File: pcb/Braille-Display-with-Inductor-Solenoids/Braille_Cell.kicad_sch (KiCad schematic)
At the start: 43 parts, among them U10 AD116, U11 AD116, U12 AD116, U13 AD116, U8 AD116, U9 AD116

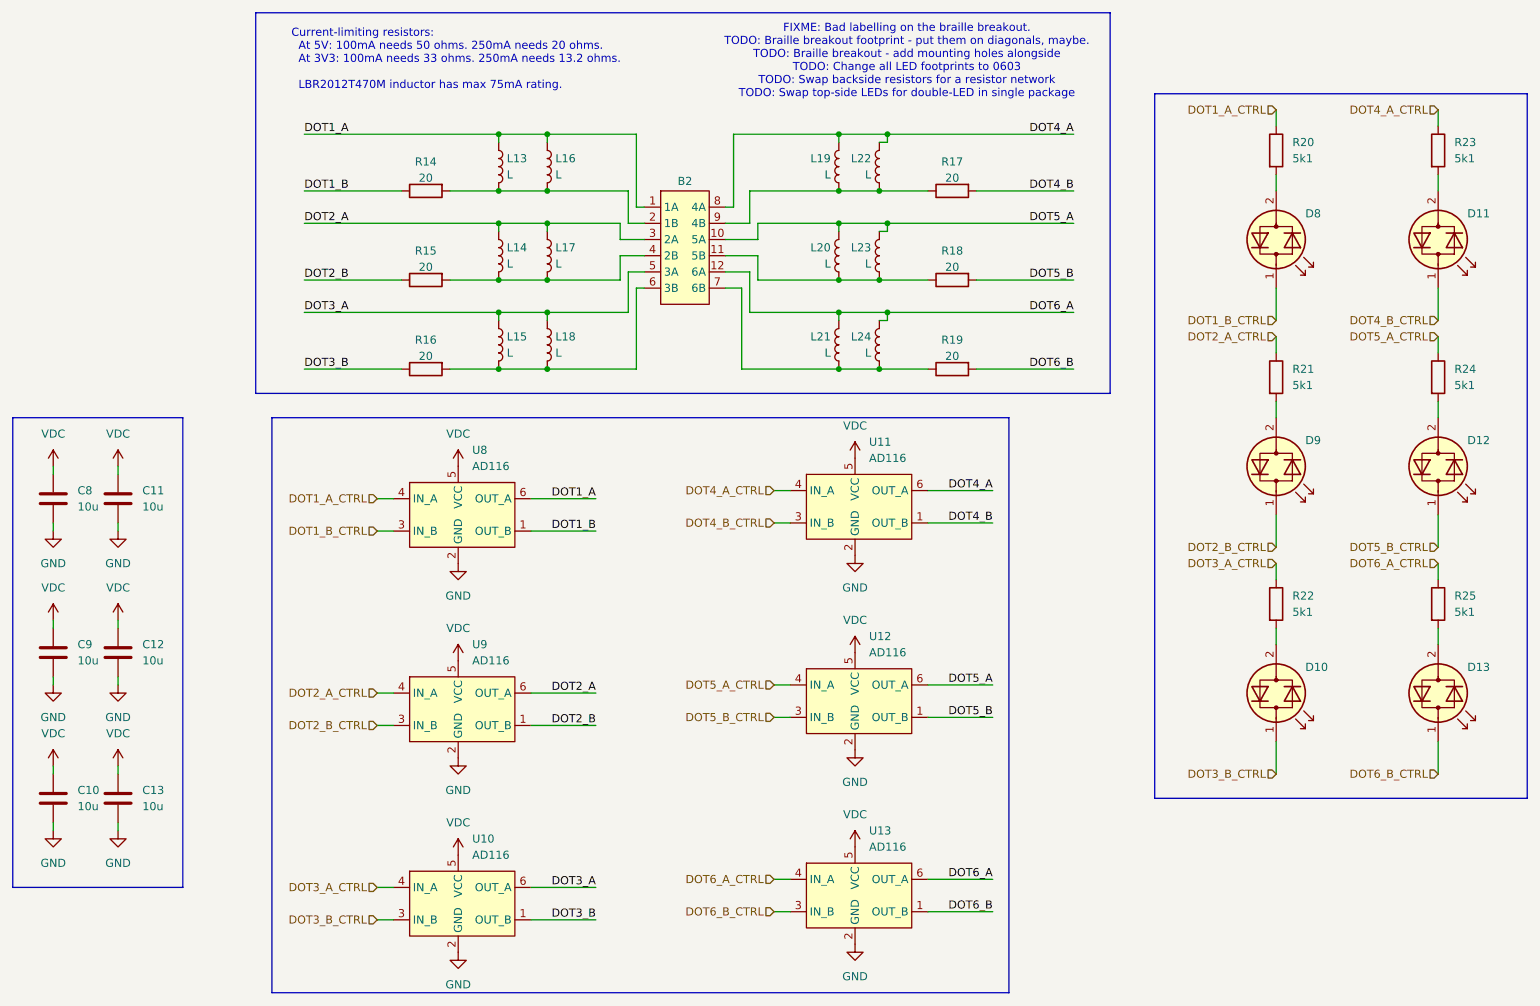
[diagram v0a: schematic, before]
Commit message: PCB (Rev 3): Switch to 2 inductors per cell (#2)
* WIP (Rev3): Switch to 2 inductors per cell

* WIP: Route one cell

* WIP: Route more of the board

* WIP: Swap around power input placement

* Finish and polish design

* Bit of tiny routing, export production file
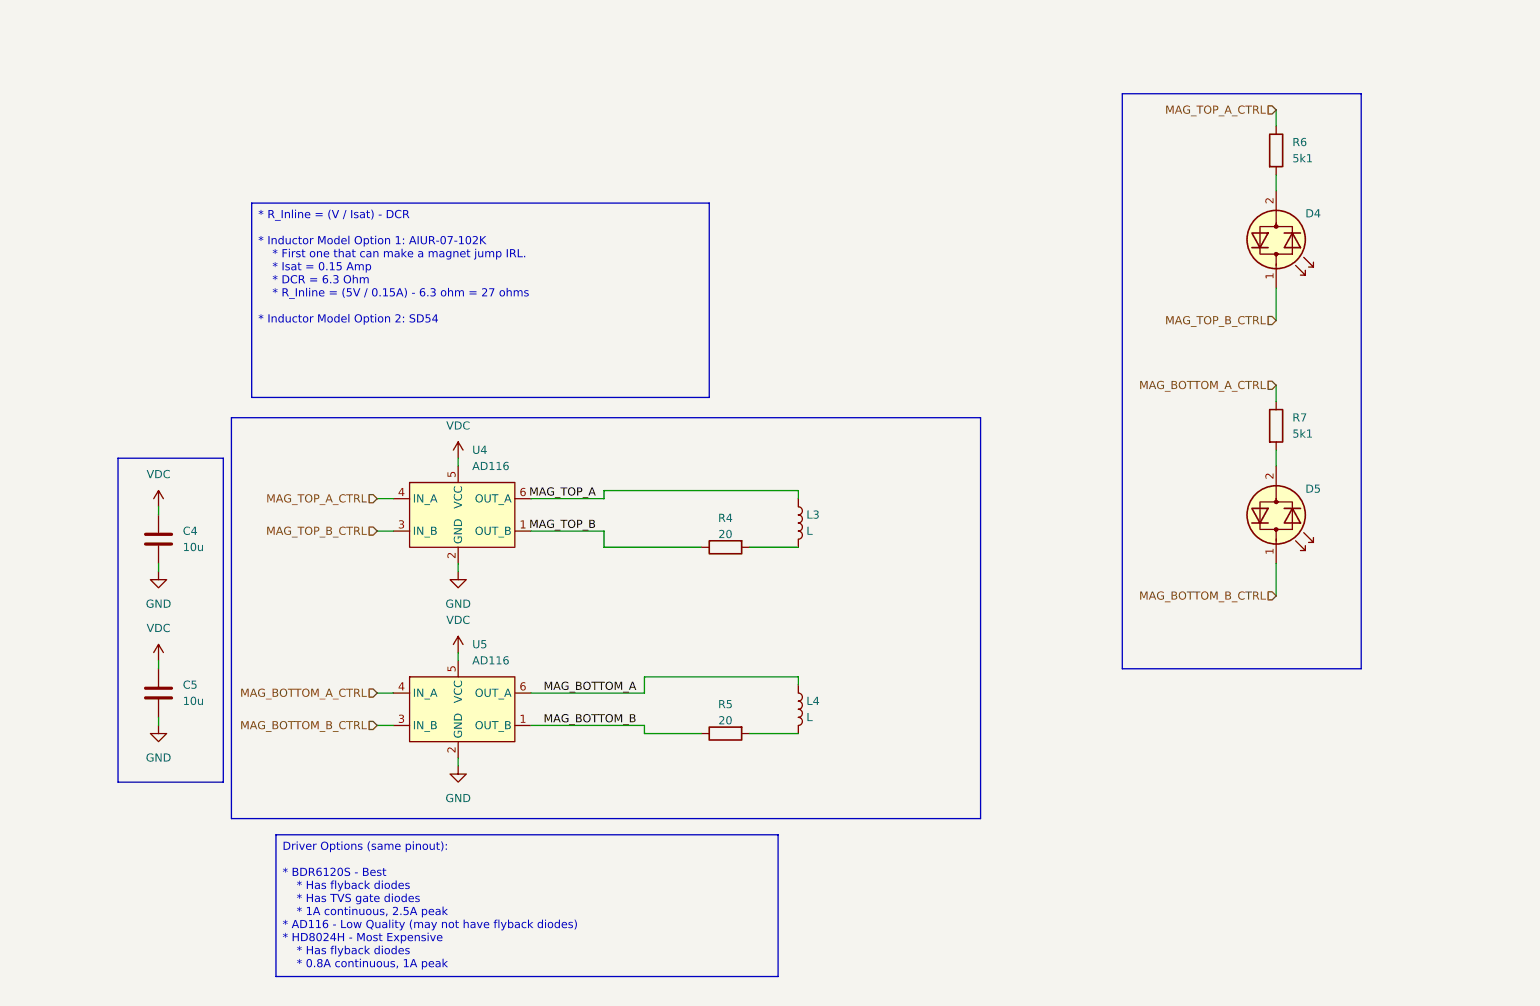
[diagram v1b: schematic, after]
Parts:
- removed B2: ~, 00-project-footprints:Braille_Cell_Breakout, symbol 00-project-symbols:Braille_Cell_Breakout
- removed C10, C11, C12, C13: 10u, Capacitor_SMD:C_1206_3216Metric_Pad1.33x1.80mm_HandSolder, symbol Device:C
- removed D10, D11, D12, D13: LED_Dual_Bidirectional, 00-project-footprints:LED_0603_1608Metric_HandSolder_2x_Reverse, symbol Device:LED_Dual_Bidirectional
- removed L15, L22, L23, L24: L, 00-project-footprints:Inductor_0805_2012Metric_SMD_Vertical_Square_Rev2_1.3mm, symbol Device:L
- removed L16, L17, L18, L19, L20, L21: L, 00-project-footprints:Inductor_VLS201612CX, symbol Device:L
- removed R16, R17, R18, R19: 20, Resistor_SMD:R_0603_1608Metric_Pad0.98x0.95mm_HandSolder, symbol Device:R
- removed R22, R23, R24, R25: 5k1, Resistor_SMD:R_0603_1608Metric_Pad0.98x0.95mm_HandSolder, symbol Device:R
- removed U10, U11, U12, U13: AD116, Package_TO_SOT_SMD:SOT-23-6, symbol 00-project-symbols:AD116_H_Bridge
- L3: renamed from L13; footprint 00-project-footprints:Inductor_0805_2012Metric_SMD_Vertical_Square_Rev2_1.3mm -> 00-project-footprints:Inductor_6mm_AIUR-07-102K_THT_SD54_SMD
- L4: renamed from L14; footprint 00-project-footprints:Inductor_0805_2012Metric_SMD_Vertical_Square_Rev2_1.3mm -> 00-project-footprints:Inductor_6mm_AIUR-07-102K_THT_SD54_SMD
- R4: renamed from R14; footprint Resistor_SMD:R_0603_1608Metric_Pad0.98x0.95mm_HandSolder -> Resistor_SMD:R_2512_6332Metric_Pad1.40x3.35mm_HandSolder
- R5: renamed from R15; footprint Resistor_SMD:R_0603_1608Metric_Pad0.98x0.95mm_HandSolder -> Resistor_SMD:R_2512_6332Metric_Pad1.40x3.35mm_HandSolder
- renumbered C8 to C4, C9 to C5, D8 to D4, D9 to D5, R20 to R6, R21 to R7, U8 to U4, U9 to U5
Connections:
- net DOT1_A renamed MAG_TOP_A
- net DOT1_A_CTRL renamed MAG_TOP_A_CTRL
- net DOT1_B renamed MAG_TOP_B
- net DOT1_B_CTRL renamed MAG_TOP_B_CTRL
- net DOT2_A renamed MAG_BOTTOM_A
- net DOT2_A_CTRL renamed MAG_BOTTOM_A_CTRL
- net DOT2_B renamed MAG_BOTTOM_B
- net DOT2_B_CTRL renamed MAG_BOTTOM_B_CTRL
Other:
- note removed: "Current-limiting resistors: At 5V: 100mA needs 50 ohms. 250mA needs 20 ohms. At 3V3: 100mA needs 33 ohms. 250mA needs 13.2 ohms. LBR2012T470M inductor has max 75mA rating."
- note removed: "FIXME: Bad labelling on the braille breakout. TODO: Braille breakout footprint - put them on diagonals, maybe. TODO: Braille breakout - add mounting holes alongside TODO: Change all LED footprints to 0603 TODO: Swap backside resistors for a resistor network TODO: Swap top-side LEDs for double-LED in single package"
- moved on the sheet: C4, C5, D5, L3, L4, R4, R5, R7
